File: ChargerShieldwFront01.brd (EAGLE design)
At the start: 158.8 x 147.3 mm, 89 parts, among them IC1 TL431, IC2 LM324N, Q1 BUZ11, Q2 BD648, Q3 BUZ171, Q4 BUZ11, Q5 BD648, Q6 BUZ171, T1 BC548, T2 BC548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

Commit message: upd
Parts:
- R25: device rcl:0207/12 -> rcl:0207/10
- R27: device rcl:0207/10 -> rcl:0207/12
- R28: device rcl:0207/10 -> rcl:0207/15
- moved R36 55.9 mm to (8.89, -24.1), turned to 90 degrees
- moved R41 18.5 mm to (-5.08, 10.2), turned to 180 degrees
- moved C9 15.5 mm to (-2.54, 15.2), turned to 0 degrees
- moved R40 10.5 mm to (-12.7, 19.1)
- moved R28 9.16 mm to (2.54, 53.3)
- moved R29 9.16 mm to (-5.08, 48.3), turned to 180 degrees
- moved R37 3.59 mm to (15.2, 30.5), turned to 0 degrees
- moved C6 2.54 mm to (0.00, 22.9), turned to 0 degrees
- moved C8 2.54 mm to (0.00, 27.9), turned to 0 degrees
- moved IC1 1.27 mm to (12.7, 38.1)
- moved R25 1.27 mm to (6.35, 43.2)
- moved R27 1.27 mm to (-24.1, 17.8)
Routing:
- net VCC: track 36.9 -> 266.7 mm
- net N$40: track 0.00 -> 94.0 mm
- net N$44: track 0.00 -> 90.0 mm
- net N$45: track 0.00 -> 61.1 mm
- net N$48: track 18.8 -> 67.9 mm
- net N$49: track 0.00 -> 47.7 mm
- net N$46: track 0.00 -> 35.6 mm
- net I_SENSE2: track 0.00 -> 32.9 mm
- net PWM_CHARGE2: track 0.00 -> 26.9 mm, vias 0 -> 2
- net N$39: track 0.00 -> 22.2 mm
- net N$51: track 0.00 -> 20.3 mm
- net N$41: track 0.00 -> 18.1 mm
- net U_BATT2: track 0.00 -> 13.5 mm
- net N$43: track 0.00 -> 12.7 mm
- net N$37: track 0.00 -> 11.8 mm
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
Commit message: thicker wires
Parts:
- moved R36 30.5 mm to (8.89, 6.35)
- moved X2 26.1 mm to (96.5, 64.8), turned to 180 degrees
- moved R26 16.1 mm to (-35.6, 20.3), turned to 90 degrees
- moved X3 14.0 mm to (73.7, 64.8)
- moved JP1 10.2 mm to (61.0, 64.8)
- moved U$1 10.2 mm to (54.6, 67.9)
- moved R9 9.25 mm to (72.4, 12.7)
- moved Q1 8.03 mm to (63.5, 19.1)
- moved R11 7.73 mm to (63.5, 40.6)
- moved R12 7.73 mm to (68.6, 40.6)
- moved D2 7.73 mm to (81.3, 20.3)
- moved R38 7.73 mm to (8.89, 35.6), turned to 270 degrees
- moved C3 7.62 mm to (73.7, 25.4)
- moved JP2 7.62 mm to (77.5, 15.2)
- moved JP3 7.62 mm to (87.6, 15.2)
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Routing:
- net U_BATT2: track 13.5 -> 95.8 mm
- net N$40: track 94.0 -> 44.4 mm
- net I_BATT2: track 10.8 -> 59.7 mm
- net VCC: track 266.7 -> 311.3 mm
- net N$42: track 4.02 -> 43.2 mm, vias 0 -> 2
- net N$51: track 20.3 -> 50.6 mm
- net N$9: track 34.9 -> 55.0 mm
- net N$7: track 56.1 -> 73.2 mm
- net GND: track 15.4 -> 31.3 mm, vias 2 -> 4
- net N$8: track 59.5 -> 71.0 mm
- net N$18: track 49.6 -> 39.4 mm
- net N$25: track 24.2 -> 34.1 mm
- net N$39: track 22.2 -> 31.8 mm
- net N$41: track 18.1 -> 26.9 mm
- net I_SENSE: track 62.0 -> 53.3 mm
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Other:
- outline, holes or cut-outs redrawn

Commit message: upd
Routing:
- net N$46: track 35.2 -> 34.5 mm
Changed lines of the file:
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@@
 <wire x1="8.255" y1="29.21" x2="13.97" y2="29.21" width="0.6604" layer="16"/>
 <wire x1="13.97" y1="29.21" x2="15.24" y2="27.94" width="0.6604" layer="16"/>
-<wire x1="15.24" y1="27.94" x2="20.32" y2="27.94" width="0.6604" layer="16"/>
-<wire x1="20.32" y1="27.94" x2="20.32" y2="26.67" width="0.6604" layer="16"/>
+<wire x1="15.24" y1="27.94" x2="19.05" y2="27.94" width="0.6604" layer="16"/>
+<wire x1="19.05" y1="27.94" x2="20.32" y2="26.67" width="0.6604" layer="16"/>
 <wire x1="20.32" y1="26.67" x2="22.86" y2="26.67" width="0.6604" layer="16"/>
 <wire x1="1.27" y1="34.29" x2="8.255" y2="29.21" width="0.6604" layer="16"/>

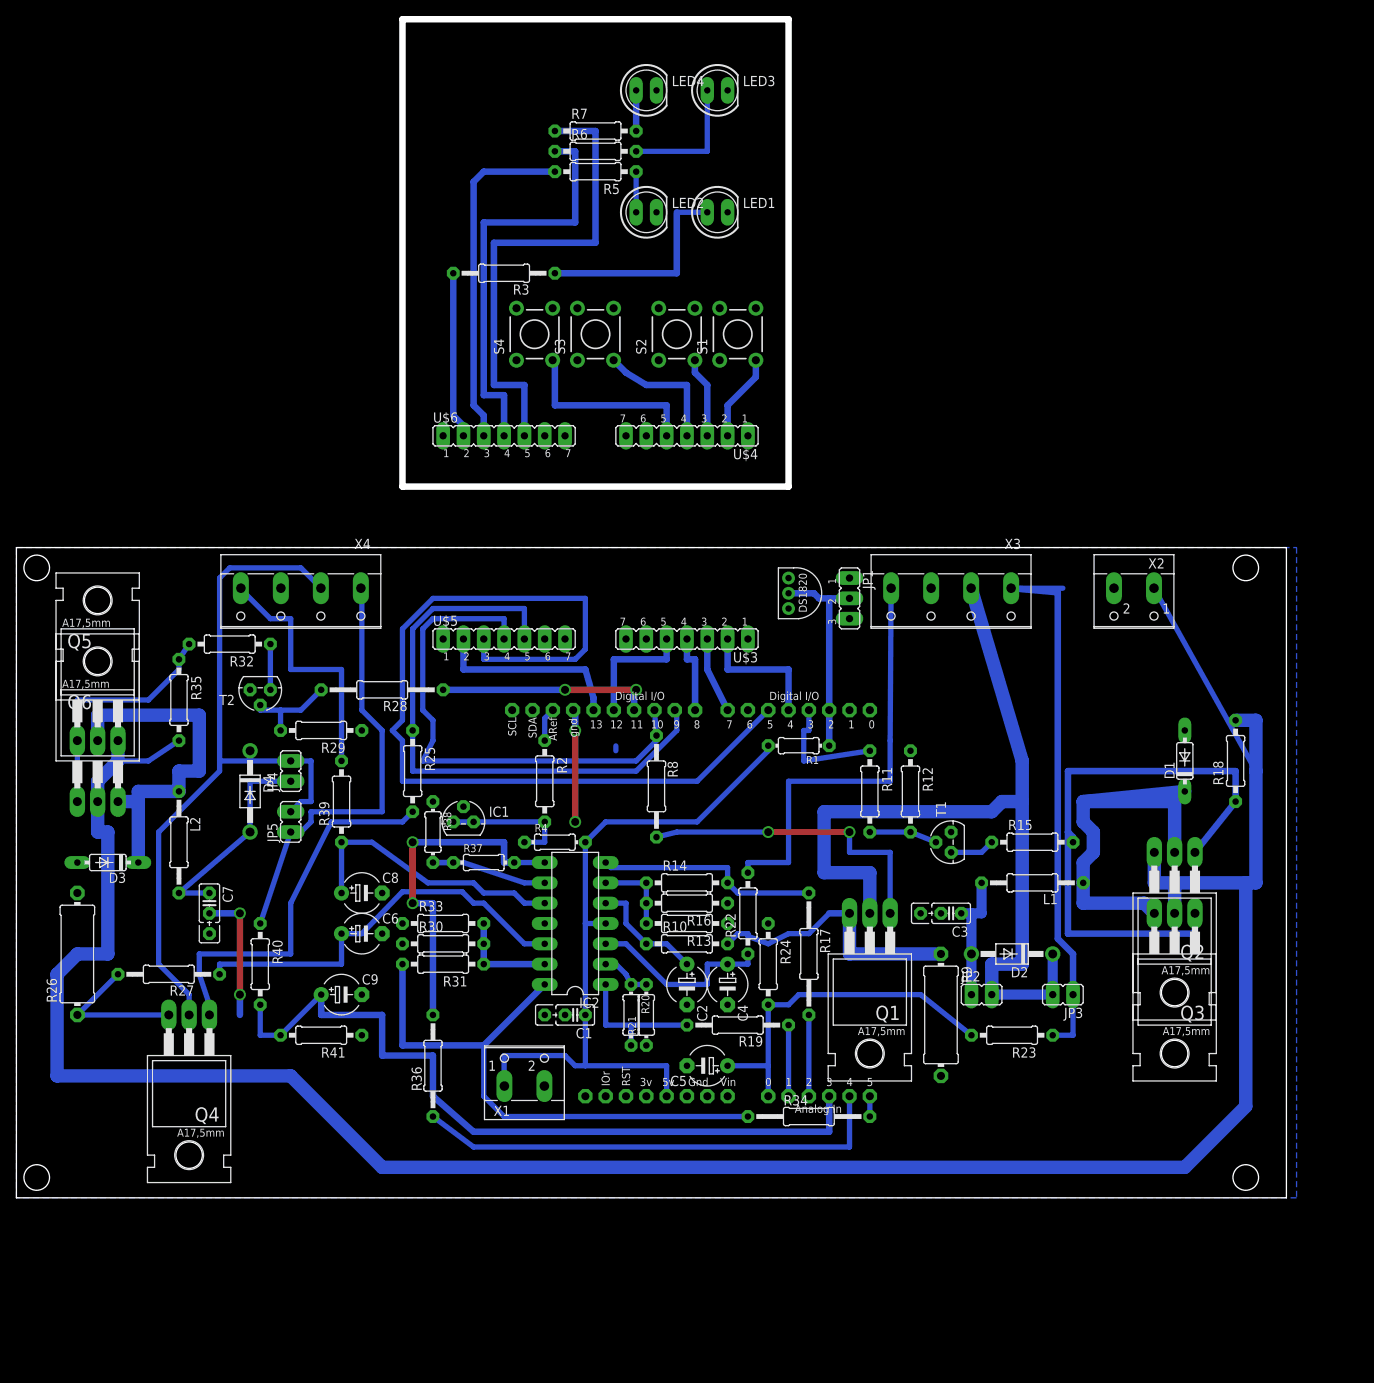
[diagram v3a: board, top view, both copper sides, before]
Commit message: difference amplifier at charge current
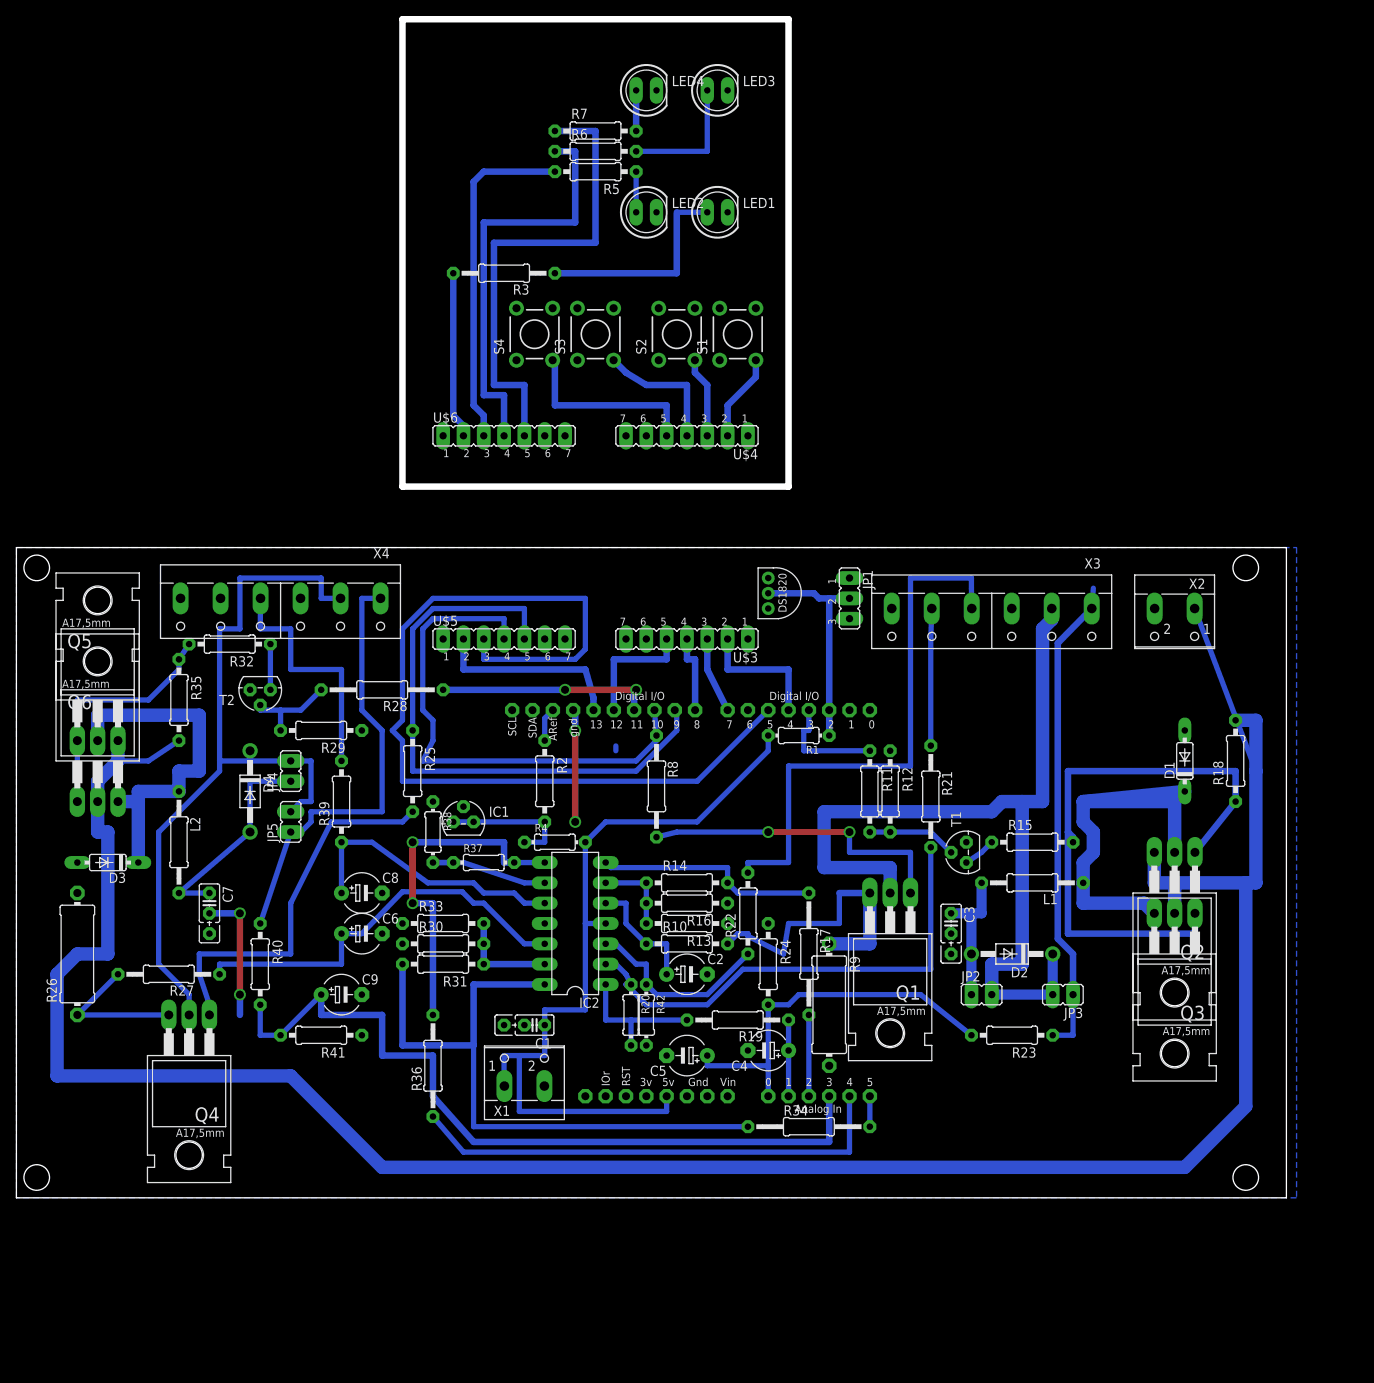
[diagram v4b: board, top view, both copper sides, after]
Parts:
- added R42: 100k, rcl:0204/7
- Q1, Q4: value BUZ11 -> BUZ11BH; device transistor-fet:TO220 -> transistor-power:TO220BH
- R21: device rcl:0204/7 -> rcl:0207/12
- R22: value 1k -> 10k
- X3, X4: device con-wago-500:W237-4 -> con-wago-500:W237-6
- moved R21 44.8 mm to (71.1, 40.0), turned to 270 degrees
- moved R9 14.0 mm to (58.4, 14.0)
- moved C4 9.69 mm to (50.8, 8.26), turned to 180 degrees
- moved X2 5.68 mm to (101.6, 62.2)
- moved X3 5.68 mm to (78.7, 62.2)
- moved C1 5.24 mm to (21.6, 11.4)
- moved Q1 3.59 mm to (66.0, 21.6)
- moved C5 2.84 mm to (40.6, 7.62)
- moved X4 2.84 mm to (-10.2, 63.5)
- moved U$1 2.54 mm to (52.1, 67.9)
- moved R12 2.54 mm to (66.0, 40.6)
- moved T1 2.29 mm to (75.6, 33.0)
- moved R1 1.27 mm to (54.6, 47.6)
- moved R34 1.27 mm to (55.9, -1.27)
- moved C2 1.27 mm to (40.6, 17.8), turned to 0 degrees
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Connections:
- net I_SENSE renamed I1_SENSE+
- net N$8 renamed U1_SENSE+
- new net I1_SENSE-: R21.1, X3.5
- net GND: now also R42.2, X3.6, X4.6; no longer R21.1, X4.3
- net I_BATT1: now also C4.+
- net N$13: now also Q1.D; no longer Q1.2
- net N$15: now also R42.1; no longer C4.+
- net N$18: now also Q1.G; no longer Q1.1
- net N$25: now also Q1.S; no longer Q1.3
- net N$44: now also Q4.D; no longer Q4.2
- net N$49: now also Q4.G; no longer Q4.1
- net N$50: now also Q4.S; no longer Q4.3
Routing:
- net N$14: track 6.39 -> 61.4 mm
- net I1_SENSE-: track 0.00 -> 17.3 mm
- net I1_SENSE+: track 53.3 -> 68.6 mm
- net +5V: track 87.2 -> 100.0 mm
- net U1_SENSE+: track 71.0 -> 61.0 mm
- net N$48: track 71.5 -> 80.0 mm
- net VCC: track 311.3 -> 306.8 mm
- net U_BATT1: track 44.2 -> 48.0 mm
- net N$25: track 34.1 -> 37.6 mm
- net N$44: track 94.5 -> 97.9 mm
- net N$5: track 8.50 -> 11.2 mm
- net U_BATT2: track 95.8 -> 98.0 mm
- net I_SENSE2: track 32.2 -> 30.5 mm
- net N$6: track 5.61 -> 4.09 mm
- net I_BATT2: track 59.7 -> 61.1 mm
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
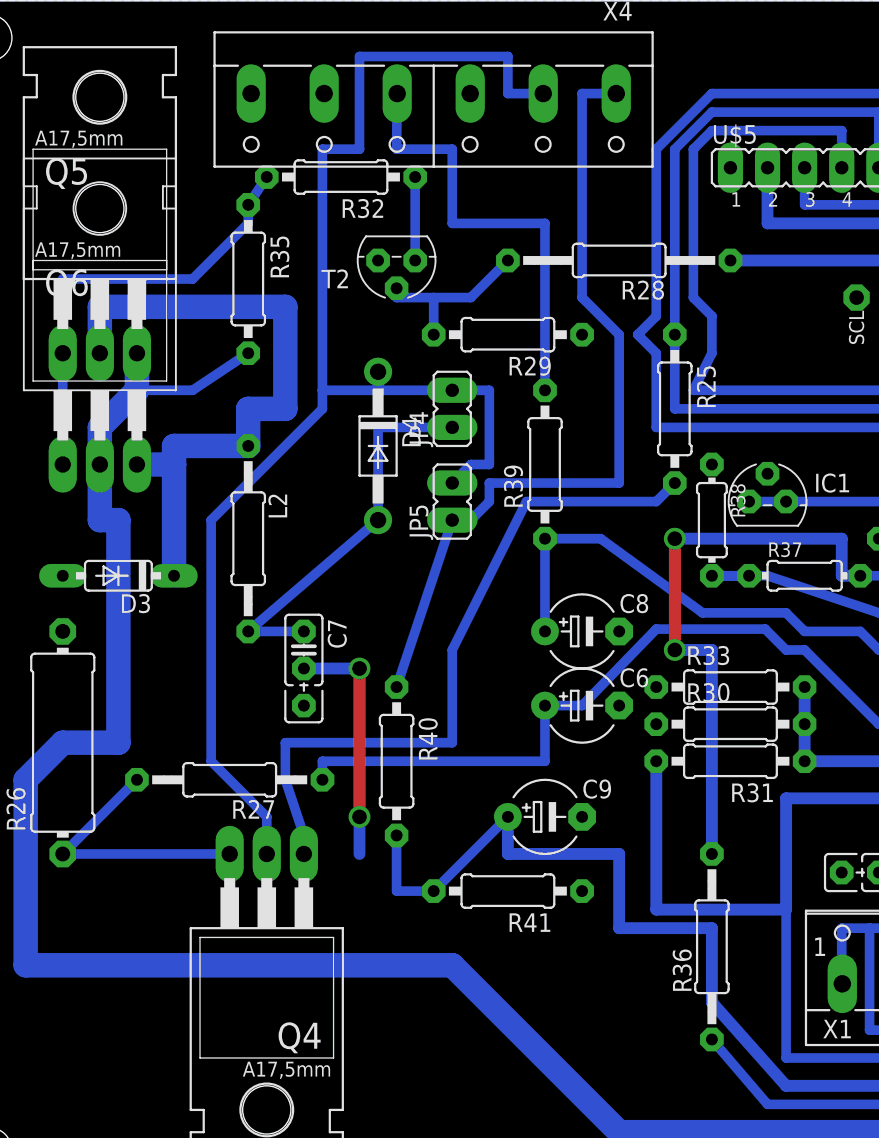
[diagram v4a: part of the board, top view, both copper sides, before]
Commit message: all I_batt differential
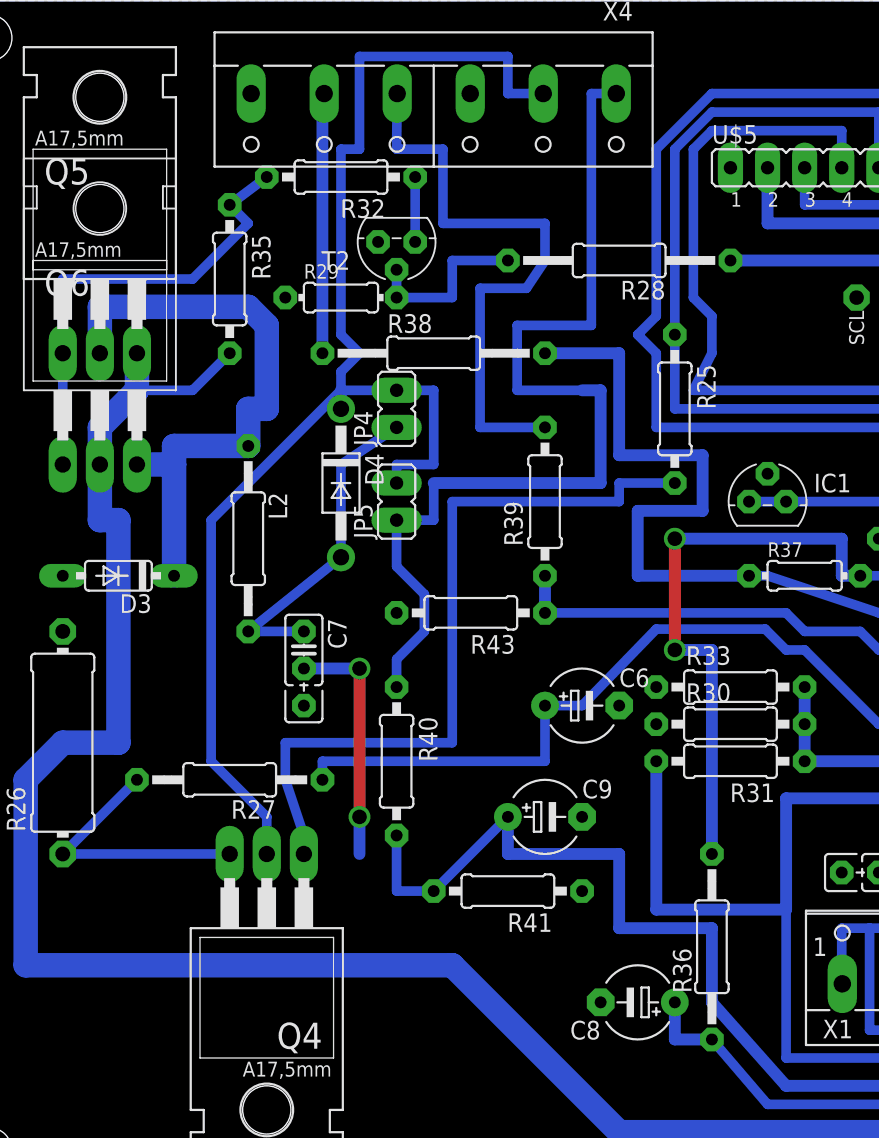
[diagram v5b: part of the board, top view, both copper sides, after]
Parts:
- added R43: 100k, rcl:0207/10
- R29: device rcl:0207/10 -> rcl:0204/7
- R38: device rcl:0204/7 -> rcl:0207/15
- R39: value 1k -> 10k
- moved C8 25.7 mm to (3.81, 2.54), turned to 180 degrees
- moved R38 22.2 mm to (-10.2, 47.0), turned to 0 degrees
- moved R29 11.7 mm to (-16.5, 50.8), turned to 0 degrees
- moved JP4 3.81 mm to (-12.7, 43.2)
- moved JP5 3.81 mm to (-12.7, 36.8)
- moved D4 3.59 mm to (-16.5, 38.1)
- moved R39 2.54 mm to (-2.54, 36.8)
- moved R35 1.27 mm to (-24.1, 52.1)
- moved T2 1.27 mm to (-12.7, 54.6)
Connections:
- net I_SENSE2 renamed I2_SENSE+
- new net I2_SENSE-: R38.1, X4.5
- net GND: now also R43.2; no longer R38.1
- net I_BATT2: now also C8.+
- net N$46: now also R43.1; no longer C8.+
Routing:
- net N$43: track 16.9 -> 49.9 mm
- net I2_SENSE-: track 0.00 -> 17.9 mm
- net N$45: track 55.3 -> 68.7 mm
- net I2_SENSE+: track 30.5 -> 41.0 mm
- net N$46: track 34.5 -> 29.0 mm
- net I_BATT2: track 61.1 -> 66.2 mm
- net N$49: track 47.7 -> 52.3 mm
- net N$41: track 26.9 -> 22.9 mm
- net N$44: track 97.9 -> 93.8 mm
- net N$40: track 44.4 -> 41.2 mm
- net N$39: track 31.8 -> 33.2 mm
- net N$38: track 5.71 -> 4.45 mm
- net VCC: track 306.8 -> 305.8 mm
